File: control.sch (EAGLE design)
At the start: 69 parts, among them IC2 XMEGA16A4A, IC3 LM317MBSTT3, IC5 LM358N, Q1 BSS123, Q2 BSS123, Q3 BC548, Q4 BC557C, Q5 TIP41C, Q6 TIP42C, Q7 BC338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

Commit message: small improvements
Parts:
- added C11: 100n, resistor:C-EUC0805
- added D1: (no value), diode:DIODE-DO41-7.6
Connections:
- net +12V: now also C11.2, D1.C
- net ADC4: now also D1.A
- net GND: now also C11.1
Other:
- moved on the sheet: C8, C9, IC5A, IC5B, JP3, Q3, Q4, Q5, Q6, Q7, R13, R3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

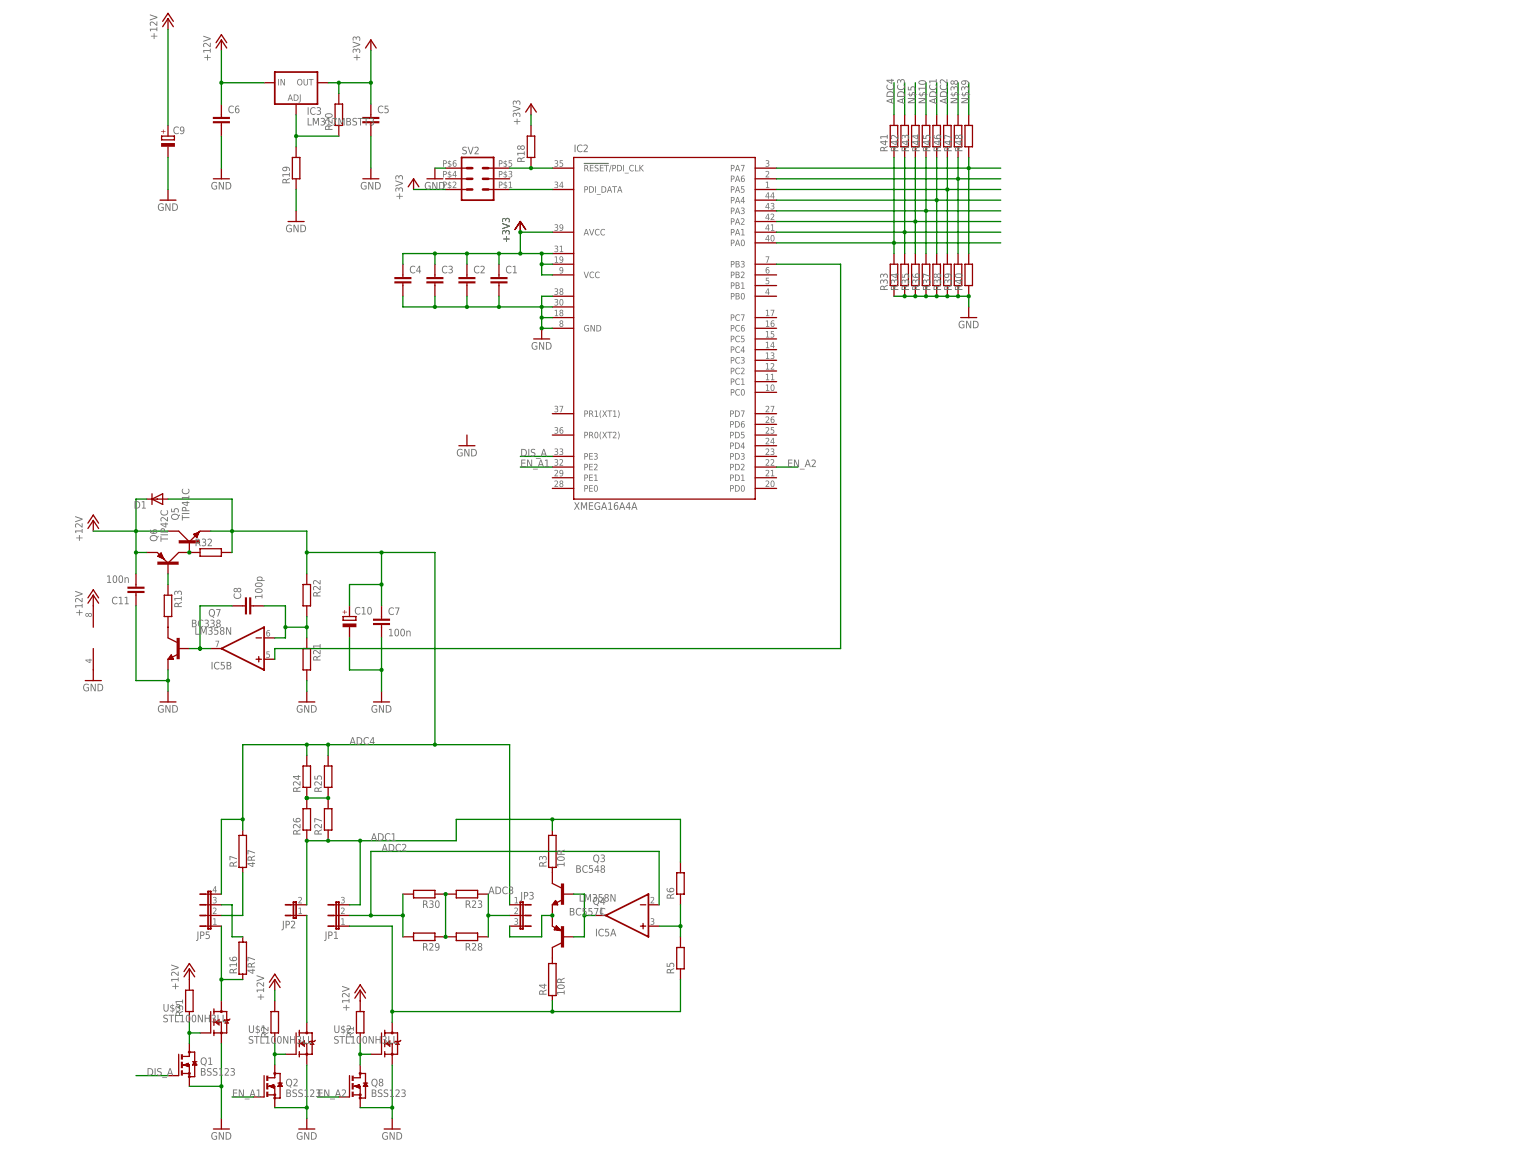
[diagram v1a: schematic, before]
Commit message: duplicated balancer and voltager regulator
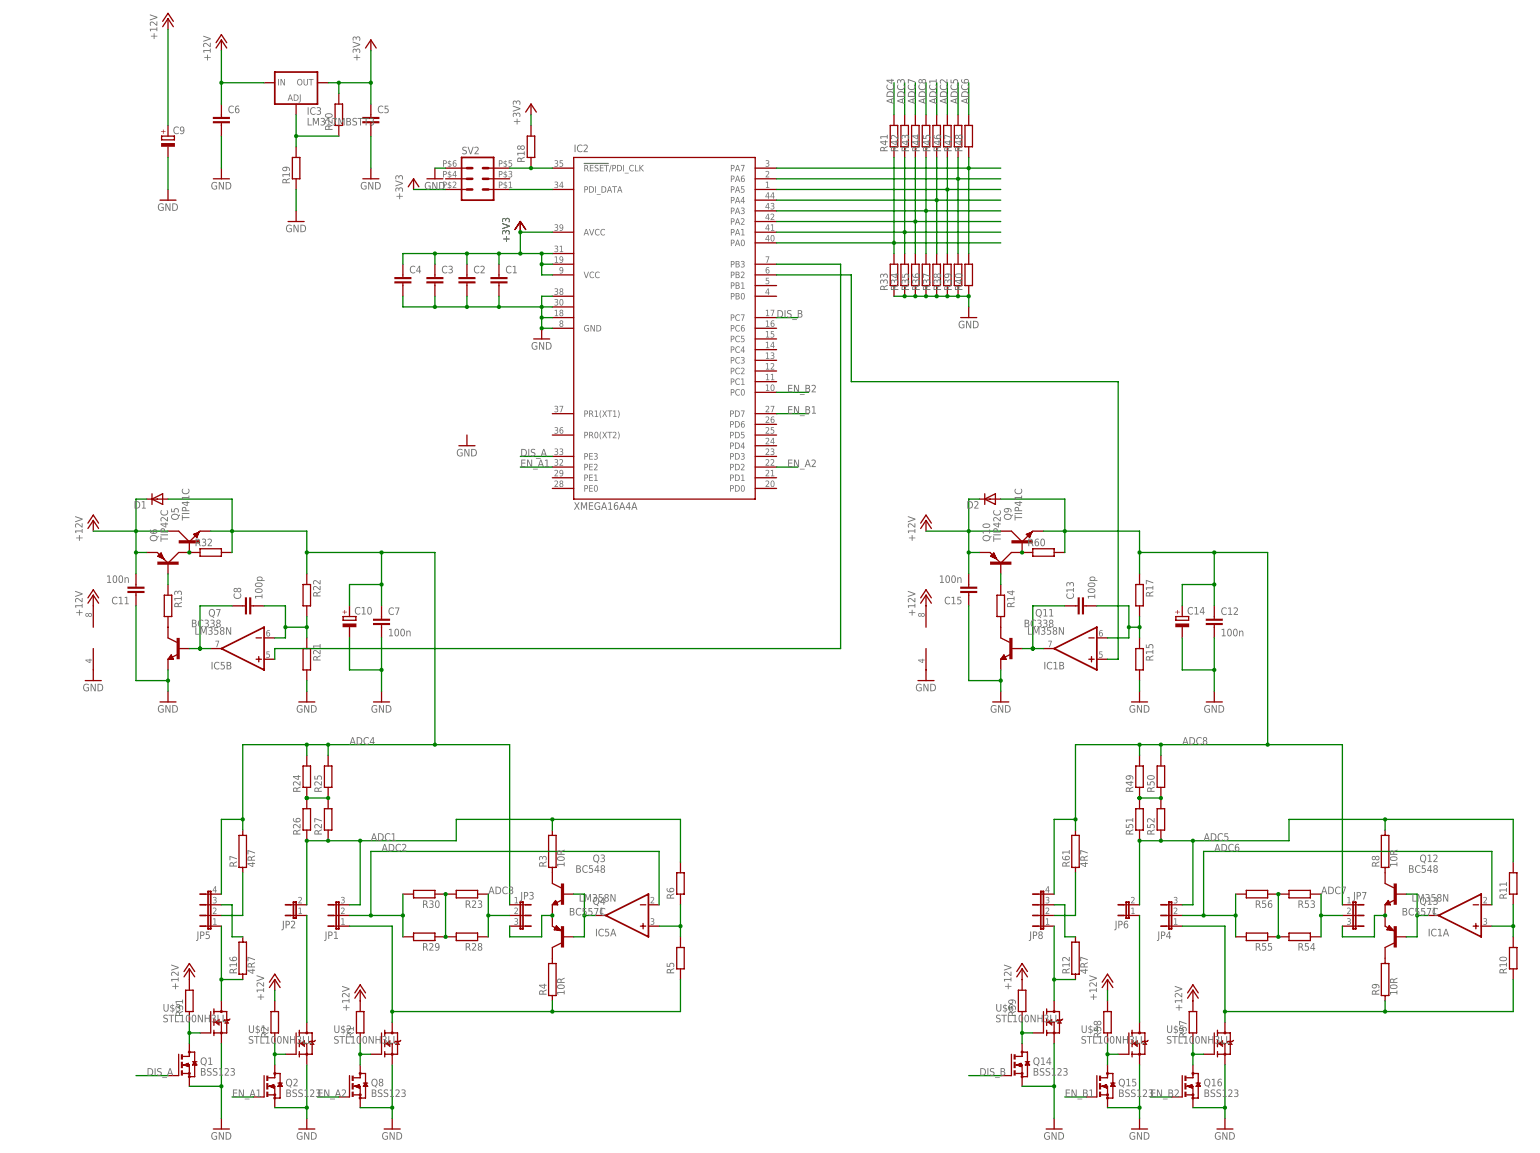
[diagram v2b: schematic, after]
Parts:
- added C12: 100n, resistor:C-EUC0805K
- added C13: 100p, resistor:C-EUC0805K
- added C14: (no value), resistor:CPOL-EUE2.5-7
- added C15: 100n, resistor:C-EUC0805
- added D2: (no value), diode:DIODE-DO41-7.6
- added IC1: LM358N, linear:LM358N
- added JP4, JP7: (no value), jumper:JP2E
- added JP6: (no value), jumper:JP1E
- added JP8: (no value), jumper:JP4E
- added Q10: TIP42C, transistor-power:TIP42C
- added Q11: BC338, transistor-npn:BC338
- added Q12: BC548, transistor-npn:BC548
- added Q13: BC557C, transistor-pnp:BC557C
- added Q14, Q15, Q16: BSS123, transistor-small-signal:BSS123
- added Q9: TIP41C, transistor-power:TIP41C
- added R10, R11, R14, R15, R17, R57, R58, R59, R60: (no value), resistor:R-EU_M0805
- added R12, R61: 4R7, resistor-power:RKH208-8R
- added R49, R50, R51, R52, R53, R54, R55, R56: (no value), resistor:R-EU_0207/2V
- added R8, R9: 10R, resistor-power:RHPS58
- added U$4, U$5, U$6: STL100NH3LL, teile:STL100NH3LL
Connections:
- removed net N$10: R44.2
- removed net N$38: R47.2
- removed net N$39: R48.2
- removed net N$5: R43.2
- new net ADC5: JP4.3, JP6.2, R11.2, R47.2, R51.1, R52.1, R8.2
- new net ADC6: IC1A.-IN, JP4.2, R48.2, R55.2, R56.2
- new net ADC7: JP7.2, R43.2, R53.1, R54.1
- new net ADC8: C12.1, C14.+, D2.A, JP7.1, JP8.4, Q9.E, R17.1, R44.2, R49.2, R50.2, R60.2, R61.2
- new net DIS_B: IC2.PC7, Q14.G
- new net EN_B1: IC2.PD7, Q15.G
- new net EN_B2: IC2.PC0, Q16.G
- new net N$12: Q12.C, R8.1
- new net N$2: JP4.1, R10.1, R9.1, U$5.D
- new net N$3: JP6.1, U$4.D
- new net N$37: Q13.C, R9.2
- new net N$40: IC1A.OUT, Q12.B, Q13.B
- new net N$41: IC1A.+IN, R10.2, R11.1
- new net N$42: JP8.1, R12.1, U$6.D
- new net N$43: JP8.3, R12.2
- new net N$45: JP8.2, R61.1
- new net N$46: C13.1, IC1B.OUT, Q11.B
- new net N$47: C13.2, IC1B.-IN, R15.1, R17.2
- new net N$48: IC1B.+IN, IC2.PB2
- new net N$49: Q10.C, Q9.B, R60.1
- new net N$50: Q11.C, R14.2
- new net N$51: Q10.B, R14.1
- new net N$52: R49.1, R50.1, R51.2, R52.2
- new net N$53: R53.2, R54.2, R55.1, R56.1
- new net N$54: JP7.3, Q12.E, Q13.E
- new net N$55: Q14.D, R59.1, U$6.G
- new net N$56: Q15.D, R58.1, U$4.G
- new net N$57: Q16.D, R57.1, U$5.G
- net +12V: now also C15.2, D2.C, IC1P.V+, Q10.E, Q9.C, R57.2, R58.2, R59.2
- net GND: now also C12.2, C14.-, C15.1, IC1P.V-, Q11.E, Q14.S, Q15.S, Q16.S, R15.2, U$4.S, U$5.S, U$6.S

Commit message: routing, voltage dividers
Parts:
- added X1, X2: (no value), con-wago-508:W237-04P
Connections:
- net ADC7: now also R44.2; no longer R43.2
- net ADC8: now also R43.2; no longer R44.2
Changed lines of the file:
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@@
 <grid distance="0.1" unitdist="inch" unit="inch" style="lines" multiple="1" display="no" altdistance="0.01" altunitdist="inch" altunit="inch"/>
 <layers>
-<layer number="1" name="Top" color="4" fill="1" visible="yes" active="no"/>
-<layer number="16" name="Bottom" color="1" fill="1" visible="yes" active="no"/>
-<layer number="17" name="Pads" color="2" fill="1" visible="yes" active="no"/>
-<layer number="18" name="Vias" color="2" fill="1" visible="yes" active="no"/>
-<layer number="19" name="Unrouted" color="6" fill="1" visible="yes" active="no"/>
-<layer number="20" name="Dimension" color="15" fill="1" visible="yes" active="no"/>
-<layer number="21" name="tPlace" color="7" fill="1" visible="yes" active="no"/>
-<layer number="22" name="bPlace" color="7" fill="1" visible="yes" active="no"/>
-<layer number="23" name="tOrigins" color="15" fill="1" visible="yes" active="no"/>
-<layer number="24" name="bOrigins" color="15" fill="1" visible="yes" active="no"/>
-<layer number="25" name="tNames" color="7" fill="1" visible="yes" active="no"/>
-<layer number="26" name="bNames" color="7" fill="1" visible="yes" active="no"/>
-<layer number="27" name="tValues" color="7" fill="1" visible="yes" active="no"/>
-<layer number="28" name="bValues" color="7" fill="1" visible="yes" active="no"/>
+<layer number="1" name="Top" color="4" fill="1" visible="no" active="no"/>
+<layer number="16" name="Bottom" color="1" fill="1" visible="no" active="no"/>
+<layer number="17" name="Pads" color="2" fill="1" visible="no" active="no"/>
+<layer number="18" name="Vias" color="2" fill="1" visible="no" active="no"/>
+<layer number="19" name="Unrouted" color="6" fill="1" visible="no" active="no"/>
+<layer number="20" name="Dimension" color="15" fill="1" visible="no" active="no"/>
+<layer number="21" name="tPlace" color="7" fill="1" visible="no" active="no"/>
+<layer number="22" name="bPlace" color="7" fill="1" visible="no" active="no"/>
+<layer number="23" name="tOrigins" color="15" fill="1" visible="no" active="no"/>
+<layer number="24" name="bOrigins" color="15" fill="1" visible="no" active="no"/>
+<layer number="25" name="tNames" color="7" fill="1" visible="no" active="no"/>
+<layer number="26" name="bNames" color="7" fill="1" visible="no" active="no"/>
+<layer number="27" name="tValues" color="7" fill="1" visible="no" active="no"/>
+<layer number="28" name="bValues" color="7" fill="1" visible="no" active="no"/>
 <layer number="29" name="tStop" color="7" fill="3" visible="no" active="no"/>
 <layer number="30" name="bStop" color="7" fill="6" visible="no" active="no"/>
@@
 <layer number="35" name="tGlue" color="7" fill="4" visible="no" active="no"/>
 <layer number="36" name="bGlue" color="7" fill="5" visible="no" active="no"/>
-<layer number="37" name="tTest" color="7" fill="1" visible="yes" active="no"/>
-<layer number="38" name="bTest" color="7" fill="1" visible="yes" active="no"/>
+<layer number="37" name="tTest" color="7" fill="1" visible="no" active="no"/>
+<layer number="38" name="bTest" color="7" fill="1" visible="no" active="no"/>
 <layer number="39" name="tKeepout" color="4" fill="11" visible="no" active="no"/>
 <layer number="40" name="bKeepout" color="1" fill="11" visible="no" active="no"/>
@@
 <layer number="44" name="Drills" color="7" fill="1" visible="no" active="no"/>
 <layer number="45" name="Holes" color="7" fill="1" visible="no" active="no"/>
-<layer number="46" name="Milling" color="3" fill="1" visible="yes" active="no"/>
-<layer number="47" name="Measures" color="7" fill="1" visible="yes" active="no"/>
-<layer number="48" name="Document" color="7" fill="1" visible="yes" active="no"/>
-<layer number="49" name="Reference" color="7" fill="1" visible="yes" active="no"/>
-<layer number="51" name="tDocu" color="7" fill="1" visible="yes" active="no"/>
-<layer number="52" name="bDocu" color="7" fill="1" visible="yes" active="no"/>
+<layer number="46" name="Milling" color="3" fill="1" visible="no" active="no"/>
+<layer number="47" name="Measures" color="7" fill="1" visible="no" active="no"/>
+<layer number="48" name="Document" color="7" fill="1" visible="no" active="no"/>
+<layer number="49" name="Reference" color="7" fill="1" visible="no" active="no"/>
+<layer number="51" name="tDocu" color="7" fill="1" visible="no" active="no"/>
+<layer number="52" name="bDocu" color="7" fill="1" visible="no" active="no"/>
 <layer number="91" name="Nets" color="2" fill="1" visible="yes" active="yes"/>
 <layer number="92" name="Busses" color="1" fill="1" visible="yes" active="yes"/>
@@
 <part name="D2" library="diode" deviceset="DIODE-" device="DO41-7.6"/>
 <part name="C15" library="resistor" deviceset="C-EU" device="C0805" value="100n"/>
+<part name="X1" library="con-wago-508" deviceset="W237-04P" device=""/>
+<part name="X2" library="con-wago-508" deviceset="W237-04P" device=""/>
 </parts>
 <sheets>
@@
 <instance part="D2" gate="G$1" x="208.28" y="157.48" rot="R180"/>
 <instance part="C15" gate="G$1" x="203.2" y="134.62" rot="R180"/>
+<instance part="X1" gate="-1" x="88.9" y="22.86"/>
+<instance part="X1" gate="-2" x="88.9" y="17.78"/>
+<instance part="X1" gate="-3" x="88.9" y="12.7"/>
+<instance part="X1" gate="-4" x="88.9" y="7.62"/>
+<instance part="X2" gate="-1" x="180.34" y="25.4"/>
+<instance part="X2" gate="-2" x="180.34" y="20.32"/>
+<instance part="X2" gate="-3" x="180.34" y="15.24"/>
+<instance part="X2" gate="-4" x="180.34" y="10.16"/>
 </instances>
 <busses>
@@
 </segment>
 <segment>
-<pinref part="R43" gate="G$1" pin="2"/>
-<wire x1="190.5" y1="248.92" x2="190.5" y2="256.54" width="0.1524" layer="91"/>
-<label x="190.5" y="251.46" size="1.778" layer="95" rot="R90"/>
+<pinref part="R44" gate="G$1" pin="2"/>
+<wire x1="193.04" y1="256.54" x2="193.04" y2="248.92" width="0.1524" layer="91"/>
+<label x="193.04" y="251.46" size="1.778" layer="95" rot="R90"/>
 </segment>
 </net>
@@
 </segment>
 <segment>
-<pinref part="R44" gate="G$1" pin="2"/>
-<wire x1="193.04" y1="256.54" x2="193.04" y2="248.92" width="0.1524" layer="91"/>
-<label x="193.04" y="251.46" size="1.778" layer="95" rot="R90"/>
-</segment>
-</net>
+<pinref part="R43" gate="G$1" pin="2"/>
+<wire x1="190.5" y1="248.92" x2="190.5" y2="256.54" width="0.1524" layer="91"/>
+<label x="190.5" y="251.46" size="1.778" layer="95" rot="R90"/>
+</segment>
+</net>

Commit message: opamp gateswap, fet driver move
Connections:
- net ADC6: now also IC1B.-IN; no longer IC1A.-IN
- net N$40: now also IC1B.OUT; no longer IC1A.OUT
- net N$41: now also IC1B.+IN; no longer IC1A.+IN
- net N$46: now also IC1A.OUT; no longer IC1B.OUT
- net N$47: now also IC1A.-IN; no longer IC1B.-IN
- net N$48: now also IC1A.+IN; no longer IC1B.+IN
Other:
- moved on the sheet: IC1A, IC1B
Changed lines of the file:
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@@
 <instance part="P+10" gate="1" x="256.54" y="40.64"/>
 <instance part="R60" gate="G$1" x="220.98" y="144.78"/>
-<instance part="IC1" gate="B" x="228.6" y="121.92" rot="R180"/>
-<instance part="IC1" gate="A" x="320.04" y="58.42" rot="R180"/>
+<instance part="IC1" gate="A" x="228.6" y="121.92" rot="R180"/>
+<instance part="IC1" gate="B" x="320.04" y="58.42" rot="R180"/>
 <instance part="IC1" gate="P" x="193.04" y="124.46"/>
 <instance part="P+11" gate="1" x="193.04" y="134.62"/>
@@
 <pinref part="Q12" gate="G$1" pin="B"/>
 <wire x1="309.88" y1="63.5" x2="307.34" y2="63.5" width="0.1524" layer="91"/>
-<pinref part="IC1" gate="A" pin="OUT"/>
+<pinref part="IC1" gate="B" pin="OUT"/>
 </segment>
 </net>
@@
 <wire x1="332.74" y1="55.88" x2="327.66" y2="55.88" width="0.1524" layer="91"/>
 <junction x="332.74" y="55.88"/>
-<pinref part="IC1" gate="A" pin="+IN"/>
+<pinref part="IC1" gate="B" pin="+IN"/>
 </segment>
 </net>
@@
 <wire x1="218.44" y1="132.08" x2="226.06" y2="132.08" width="0.1524" layer="91"/>
 <pinref part="Q11" gate="G$1" pin="B"/>
-<pinref part="IC1" gate="B" pin="OUT"/>
+<pinref part="IC1" gate="A" pin="OUT"/>
 <junction x="218.44" y="121.92"/>
 <wire x1="218.44" y1="121.92" x2="220.98" y2="121.92" width="0.1524" layer="91"/>
@@
 <junction x="241.3" y="127"/>
 <junction x="243.84" y="127"/>
-<pinref part="IC1" gate="B" pin="-IN"/>
+<pinref part="IC1" gate="A" pin="-IN"/>
 </segment>
 </net>
@@
 <wire x1="238.76" y1="185.42" x2="238.76" y2="119.38" width="0.1524" layer="91"/>
 <wire x1="238.76" y1="119.38" x2="236.22" y2="119.38" width="0.1524" layer="91"/>
-<pinref part="IC1" gate="B" pin="+IN"/>
+<pinref part="IC1" gate="A" pin="+IN"/>
 <wire x1="238.76" y1="185.42" x2="175.26" y2="185.42" width="0.1524" layer="91"/>
 <wire x1="175.26" y1="185.42" x2="175.26" y2="210.82" width="0.1524" layer="91"/>
@@
 <pinref part="R55" gate="G$1" pin="2"/>
 <wire x1="266.7" y1="58.42" x2="266.7" y2="53.34" width="0.1524" layer="91"/>
-<pinref part="IC1" gate="A" pin="-IN"/>
+<pinref part="IC1" gate="B" pin="-IN"/>
 <label x="261.62" y="73.66" size="1.778" layer="95"/>
 </segment>
